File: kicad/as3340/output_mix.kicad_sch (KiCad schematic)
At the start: 31 parts

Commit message: kicad library fix...again
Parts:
- C38, C40: value (none) -> 22p; footprint (none) -> Capacitor_SMD:C_0603_1608Metric
- R10, R65: renamed from R?; value (none) -> 1k; footprint (none) -> Resistor_SMD:R_0603_1608Metric
- R11, R14: renamed from R?; value (none) -> 100k; footprint (none) -> Resistor_SMD:R_0603_1608Metric
- R12, R7: renamed from R?; value (none) -> 120k; footprint (none) -> Resistor_SMD:R_0603_1608Metric
- R13: renamed from R?; value (none) -> 150k; footprint (none) -> Resistor_SMD:R_0603_1608Metric
- R2, R3, R5, R66, R70, R71, R73, R8: renamed from R?; value (none) -> 47k; footprint (none) -> Resistor_SMD:R_0603_1608Metric
- R59: renamed from R?; value (none) -> 24k; footprint (none) -> Resistor_SMD:R_0603_1608Metric
- R6: renamed from R?; value (none) -> 62k; footprint (none) -> Resistor_SMD:R_0603_1608Metric
- R72: renamed from R?; value (none) -> 180k; footprint (none) -> Resistor_SMD:R_0603_1608Metric
- R74: renamed from R?; value (none) -> 220k; footprint (none) -> Resistor_SMD:R_0603_1608Metric
- R75: renamed from R?; value (none) -> 360k; footprint (none) -> Resistor_SMD:R_0603_1608Metric
- R9: renamed from R?; value (none) -> 91k; footprint (none) -> Resistor_SMD:R_0603_1608Metric
- U1: renamed from U?; value (none) -> TL074; footprint (none) -> Package_SO:SOIC-14_3.9x8.7mm_P1.27mm
- U5: value (none) -> MAX333A
- U6: renamed from U?; value (none) -> AS3360; footprint (none) -> Package_SO:SOIC-14_3.9x8.7mm_P1.27mm
- U8: renamed from U?; value (none) -> DG442CY+; footprint (none) -> Package_SO:SOIC-16_3.9x9.9mm_P1.27mm
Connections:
- net GND: now also U1.12 (+), U1.3 (+); no longer U1.5 (+), U1.5 (+)
- net MIX1_INV: now also U1.9 (-); no longer U1.6 (-)
- net MIX1_NONINV: now also U1.10 (+); no longer U1.5 (+)
- net MIX2_SAW_CTRL: now also U8.16; no longer U8.9
- net VCO_SAW: now also U8.14; no longer U8.11
- net at C40.2, R11.1, R13.2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: now also U1.2 (-); no longer U1.6 (-)
- net at R14.1: now also U8.15; no longer U8.10
- net at C38.1, R2.2, R70.2: now also U1.8; no longer U1.7
- net at R2.1, R3.2: now also U1.13 (-); no longer U1.6 (-)
- net at R10.1, R3.1: now also U1.14; no longer U1.7
- net at C40.1, R66.2, R71.2: now also U1.1; no longer U1.7

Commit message: remove rescue library
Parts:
- U6: symbol as3340-rescue:AS3360-Audio -> as3340:AS3360-Audio
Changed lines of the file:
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@@
     (pin "2")
   )
-  (symbol (lib_id "as3340-rescue:AS3360-Audio") (at 232.41 134.62 0) (unit 1)
+  (symbol (lib_id "as3340:AS3360-Audio") (at 232.41 134.62 0) (unit 1)
     (in_bom yes) (on_board yes)
     (property "Reference" "U6" (id 0) (at 232.41 127 0))

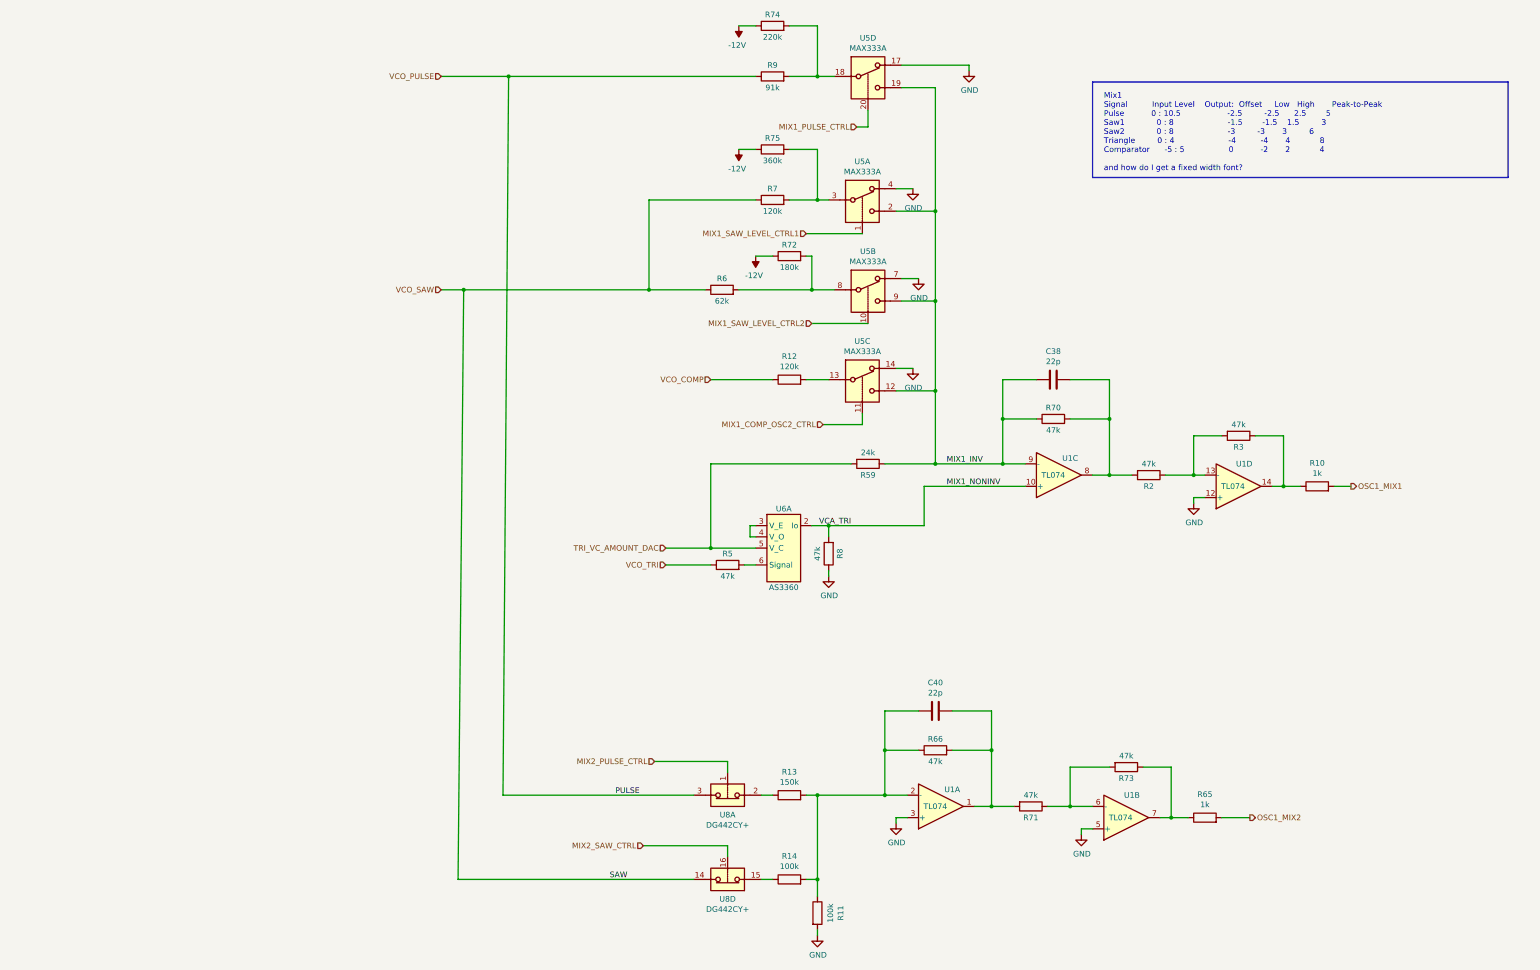
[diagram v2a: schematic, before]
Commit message: schematic changes, still need values
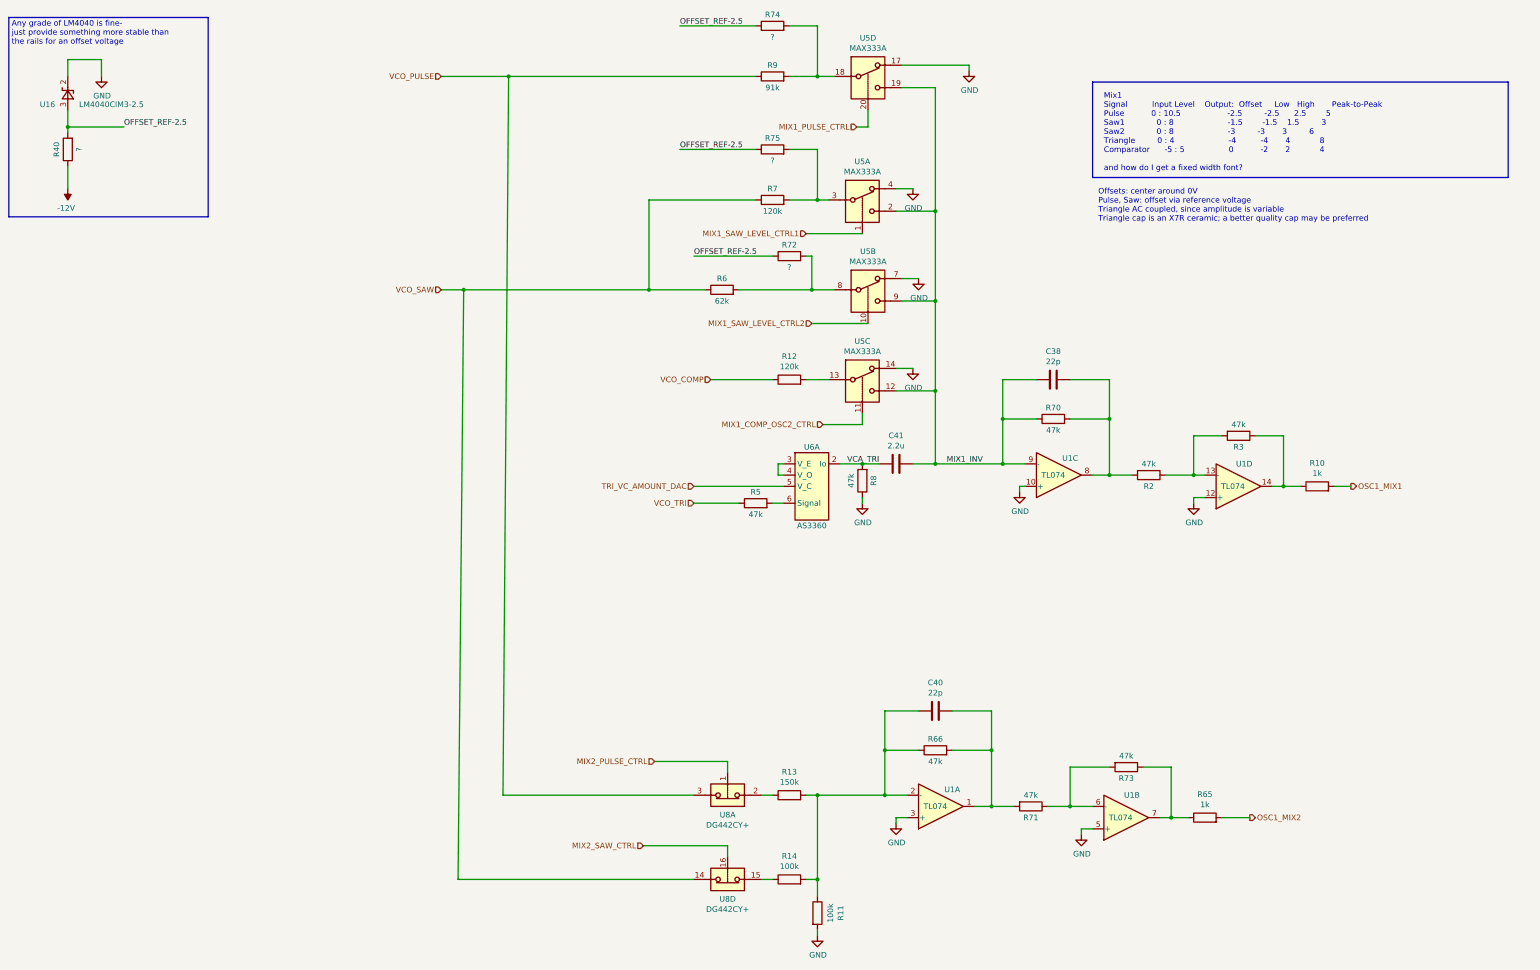
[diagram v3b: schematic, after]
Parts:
- removed R59: 24k, Resistor_SMD:R_0603_1608Metric, symbol Device:R
- added C41: 2.2u, Capacitor_SMD:C_1206_3216Metric, symbol Device:C
- added R40: ?, Resistor_SMD:R_0603_1608Metric, symbol Device:R
- added U16: LM4040CIM3-2.5, Package_TO_SOT_SMD:SOT-23, symbol Reference_Voltage:LM4040LP-4.1
- R72: value 180k -> ?; LCSC Part C22827 -> (none)
- R74: value 220k -> ?; LCSC Part C22961 -> (none)
- R75: value 360k -> ?
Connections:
- net -12V: now also R40.1; no longer R72.1, R74.1, R75.1
- net GND: now also U1.10 (+), U16.2 (K)
- net MIX1_INV: now also C41.1
- net MIX1_NONINV renamed VCA_TRI
- net VCA_TRI: now also C41.2; no longer U1.10 (+)
- new net OFFSET_REF-2.5: R40.2, R72.1, R74.1, R75.1, U16.3 (A)
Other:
- note added: "Any grade of LM4040 is fine- just provide something more stable than the rails for an offset voltage"
- note added: "Offsets: center around 0V Pulse, Saw: offset via reference voltage Triangle AC coupled, since amplitude is variable Triangle cap is an X7R ceramic; a better quality cap may be preferred"
- moved on the sheet: R5, R8, U6A

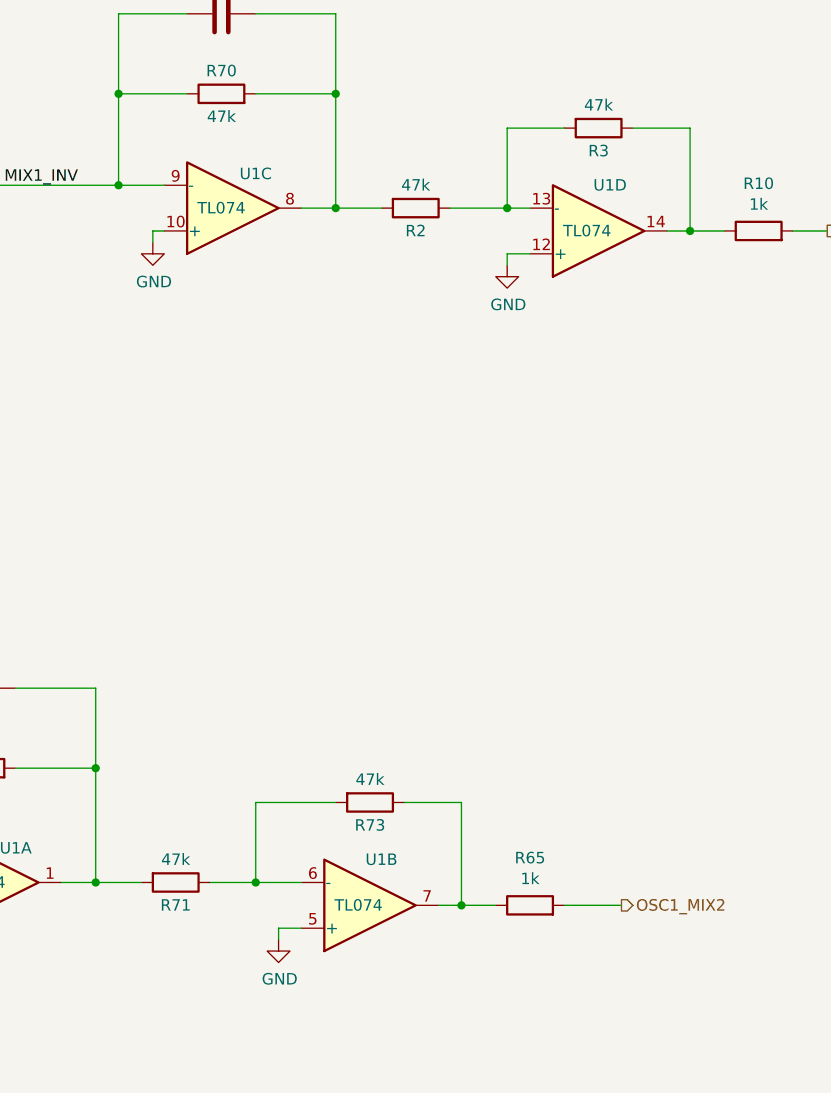
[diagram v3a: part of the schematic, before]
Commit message: moved 2x20 5mm back
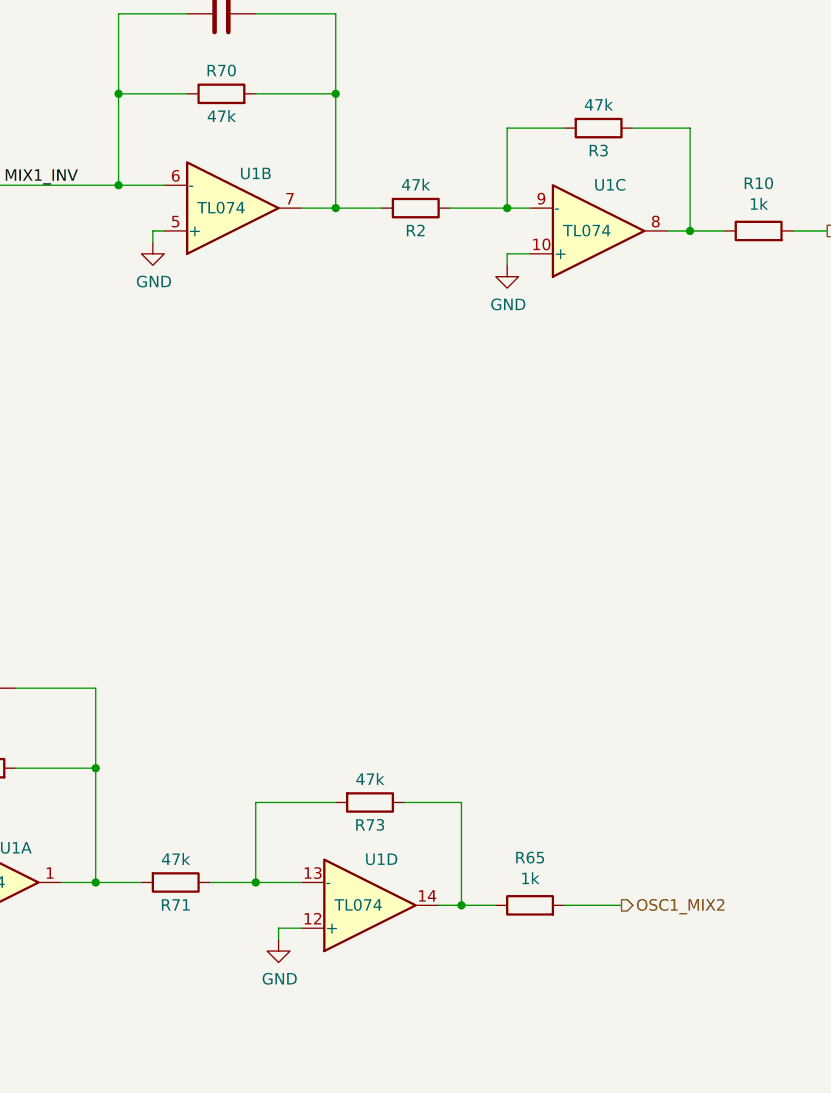
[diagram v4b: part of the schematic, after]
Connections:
- net GND: now also U1.10 (+), U1.12 (+), U1.5 (+); no longer U1.10 (+), U1.12 (+), U1.5 (+)
- net MIX1_INV: now also U1.6 (-); no longer U1.9 (-)
- net at C38.1, R2.2, R70.2: now also U1.7; no longer U1.8
- net at R2.1, R3.2: now also U1.9 (-); no longer U1.13 (-)
- net at R10.1, R3.1: now also U1.8; no longer U1.14
- net at R65.1, R73.1: now also U1.14; no longer U1.7
- net at R71.1, R73.2: now also U1.13 (-); no longer U1.6 (-)
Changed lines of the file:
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@@
     (pin "5")
   )
-  (symbol (lib_id "Amplifier_Operational:TL074") (at 294.64 119.38 0) (mirror x) (unit 3)
+  (symbol (lib_id "Amplifier_Operational:TL074") (at 294.64 119.38 0) (mirror x) (unit 2)
     (in_bom yes) (on_board yes)
     (property "Reference" "U1" (id 0) (at 297.18 115.57 0))
@@
     (pin "4")
   )
-  (symbol (lib_id "Amplifier_Operational:TL074") (at 335.28 121.92 0) (mirror x) (unit 4)
+  (symbol (lib_id "Amplifier_Operational:TL074") (at 335.28 121.92 0) (mirror x) (unit 3)
     (in_bom yes) (on_board yes)
     (property "Reference" "U1" (id 0) (at 336.55 116.84 0))
@@
     (pin "2")
   )
-  (symbol (lib_id "Amplifier_Operational:TL074") (at 309.88 196.85 0) (mirror x) (unit 2)
+  (symbol (lib_id "Amplifier_Operational:TL074") (at 309.88 196.85 0) (mirror x) (unit 4)
     (in_bom yes) (on_board yes)
     (property "Reference" "U1" (id 0) (at 311.15 191.77 0))

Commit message: minor tweaks
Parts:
- R40, R72: value ? -> 39k
- R74: value ? -> 47k; LCSC Part (none) -> C25819
- R75: value ? -> 75k
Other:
- note added: "~16k in load to OFFSET_REF-2.5 ==> 150 uA LM4040 requires 65 uA total 215 uA 44k calculated ==> 39k resistor, allowing for power supply wierdness Changing offsets to waveforms will change this value"
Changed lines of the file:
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@@
+    (effects (font (size 1.27 1.27)) (justify left bottom))
+  )
+  (text "~16k in load to OFFSET_REF-2.5 ==> 150 uA\nLM4040 requires 65 uA\ntotal 215 uA\n44k calculated ==> 39k resistor, allowing for power supply wierdness\nChanging offsets to waveforms will change this value"
+    (at 57.785 72.39 0)
     (effects (font (size 1.27 1.27)) (justify left bottom))
   )
@@
     (in_bom yes) (on_board yes)
     (property "Reference" "R74" (id 0) (at 229.87 15.24 90))
-    (property "Value" "?" (id 1) (at 229.87 20.32 90))
+    (property "Value" "47k" (id 1) (at 229.87 20.32 90))
     (property "Footprint" "Resistor_SMD:R_0603_1608Metric" (id 2) (at 229.87 19.558 90)
       (effects (font (size 1.27 1.27)) hide)
@@
       (effects (font (size 1.27 1.27)) hide)
     )
-    (property "LCSC Part" "" (id 4) (at 229.87 17.78 0)
+    (property "LCSC Part" "C25819" (id 4) (at 229.87 17.78 0)
       (effects (font (size 1.27 1.27)) hide)
     )
@@
     (in_bom yes) (on_board yes)
     (property "Reference" "R75" (id 0) (at 229.87 43.18 90))
-    (property "Value" "?" (id 1) (at 229.87 48.26 90))
+    (property "Value" "75k" (id 1) (at 229.87 48.26 90))
     (property "Footprint" "Resistor_SMD:R_0603_1608Metric" (id 2) (at 229.87 47.498 90)
       (effects (font (size 1.27 1.27)) hide)
@@
     (in_bom yes) (on_board yes)
     (property "Reference" "R72" (id 0) (at 233.68 67.31 90))
-    (property "Value" "?" (id 1) (at 233.68 72.39 90))
+    (property "Value" "39k" (id 1) (at 233.68 72.39 90))
     (property "Footprint" "Resistor_SMD:R_0603_1608Metric" (id 2) (at 233.68 71.628 90)
       (effects (font (size 1.27 1.27)) hide)
@@
     (in_bom yes) (on_board yes)
     (property "Reference" "R40" (id 0) (at 67.945 45.72 90))
-    (property "Value" "?" (id 1) (at 73.025 45.72 90))
+    (property "Value" "39k" (id 1) (at 73.025 45.72 90))
     (property "Footprint" "Resistor_SMD:R_0603_1608Metric" (id 2) (at 72.263 45.72 90)
       (effects (font (size 1.27 1.27)) hide)

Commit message: fixes for BOM
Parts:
- R40, R72: LCSC Part (none) -> C23153
- R75: LCSC Part C23146 -> C23242
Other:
- moved on the sheet: C40, R11, R13, R14, R65, R66, R71, R73, U1A, U1D, U8A, U8D

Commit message: update title block and add schematic pdf
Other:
- title: Zoxnoxious 3340 Oscillator: Output -> Zoxnoxious 3340 Oscillator
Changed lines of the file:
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@@
   (paper "B")
   (title_block
-    (title "Zoxnoxious 3340 Oscillator: Output")
-    (rev "0.3")
+    (title "Zoxnoxious 3340 Oscillator")
+    (rev "0.4")
     (company "Zoxnoxious Engineering")
   )

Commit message: add 3340 v0.4 gerbers
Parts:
- U1: LCSC Part C12594 -> C6963
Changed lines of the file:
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@@
       (effects (font (size 1.27 1.27)) hide)
     )
-    (property "LCSC Part" "C12594" (id 4) (at 294.64 119.38 0)
+    (property "LCSC Part" "C6963" (id 4) (at 294.64 119.38 0)
       (effects (font (size 1.27 1.27)) hide)
     )
@@
       (effects (font (size 1.27 1.27)) hide)
     )
-    (property "LCSC Part" "C12594" (id 4) (at 335.28 121.92 0)
+    (property "LCSC Part" "C6963" (id 4) (at 335.28 121.92 0)
       (effects (font (size 1.27 1.27)) hide)
     )
@@
       (effects (font (size 1.27 1.27)) hide)
     )
-    (property "LCSC Part" "C12594" (id 4) (at 269.24 168.91 0)
+    (property "LCSC Part" "C6963" (id 4) (at 269.24 168.91 0)
       (effects (font (size 1.27 1.27)) hide)
     )
@@
       (effects (font (size 1.27 1.27)) hide)
     )
-    (property "LCSC Part" "C12594" (id 4) (at 311.15 171.45 0)
-      (effects (font (size 1.27 1.27)) hide)
-    )
+    (property "LCSC Part" "C6963" (id 4) (at 311.15 171.45 0)
+      (effects (font (size 1.27 1.27)) hide)
+    )
